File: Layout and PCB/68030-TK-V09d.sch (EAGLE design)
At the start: 73 parts, among them IC10 74HCT245DW, IC11 74HCT245DW, IC4 74HCT245DW, IC5 74HCT245DW, IC6 74HCT245DW, IC8 74HCT245DW, IC9 74HCT245DW, X1 FABC96R

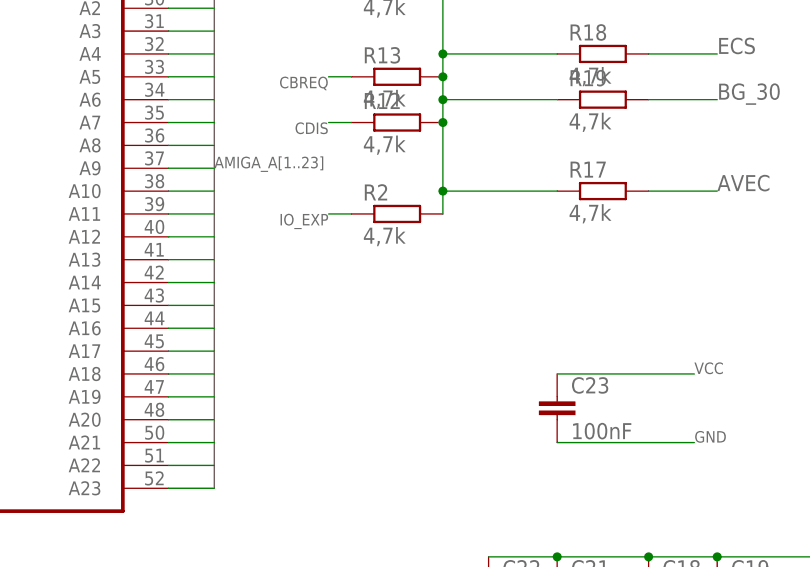
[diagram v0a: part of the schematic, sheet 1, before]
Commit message: Cache-Disable-Option on PCB
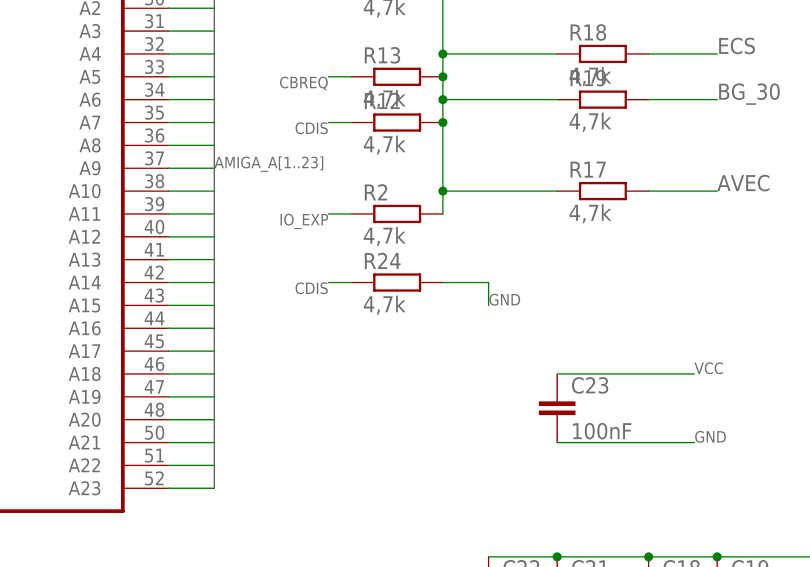
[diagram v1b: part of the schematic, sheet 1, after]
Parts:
- added R24: 4,7k, rcl:R-EU_R0603
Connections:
- net CDIS: now also R24.1
- net GND: now also R24.2
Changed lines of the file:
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@@
 <part name="R22" library="rcl" deviceset="R-EU_" device="R0603" value="4,7k"/>
 <part name="R23" library="rcl" deviceset="R-EU_" device="R0603" value="4,7k"/>
+<part name="R24" library="rcl" deviceset="R-EU_" device="R0603" value="4,7k"/>
 </parts>
 <sheets>
@@
 <instance part="R22" gate="G$1" x="-2.54" y="132.08"/>
 <instance part="R23" gate="G$1" x="-2.54" y="142.24"/>
+<instance part="R24" gate="G$1" x="-25.4" y="83.82"/>
 </instances>
 <busses>
@@
 <wire x1="132.08" y1="111.76" x2="137.16" y2="111.76" width="0.1524" layer="91"/>
 <label x="137.16" y="111.76" size="1.27" layer="95" xref="yes"/>
+</segment>
+<segment>
+<pinref part="R24" gate="G$1" pin="1"/>
+<wire x1="-30.48" y1="83.82" x2="-33.02" y2="83.82" width="0.1524" layer="91"/>
+<label x="-33.02" y="83.82" size="1.27" layer="95" rot="R180"/>
 </segment>
 </net>
@@
 <label x="7.62" y="66.04" size="1.27" layer="95"/>
 </segment>
-</net>
+<segment>
+<pinref part="R24" gate="G$1" pin="2"/>
+<wire x1="-20.32" y1="83.82" x2="-15.24" y2="83.82" width="0.1524" layer="91"/>
+<wire x1="-15.24" y1="83.82" x2="-15.24" y2="81.28" width="0.1524" layer="91"/>
+<label x="-15.24" y="81.28" size="1.27" layer="95"/>
+</segment>
+</net>

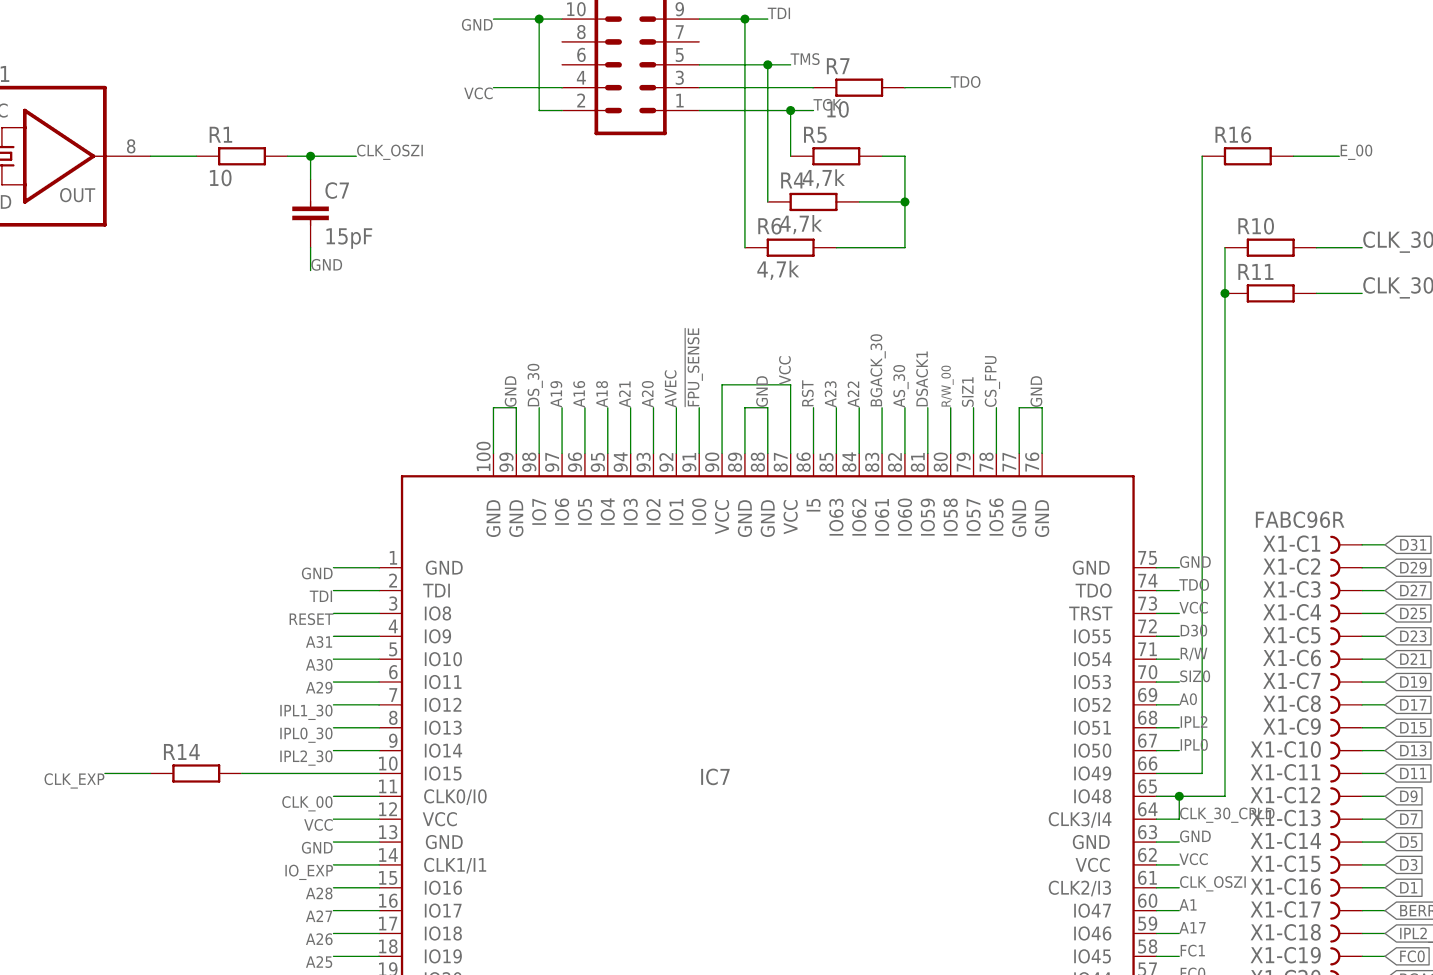
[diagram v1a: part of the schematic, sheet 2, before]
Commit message: Reset-Problem solved
The AMiga was not able to recover from a reste, because the e-clock was
not generated properly during reste.
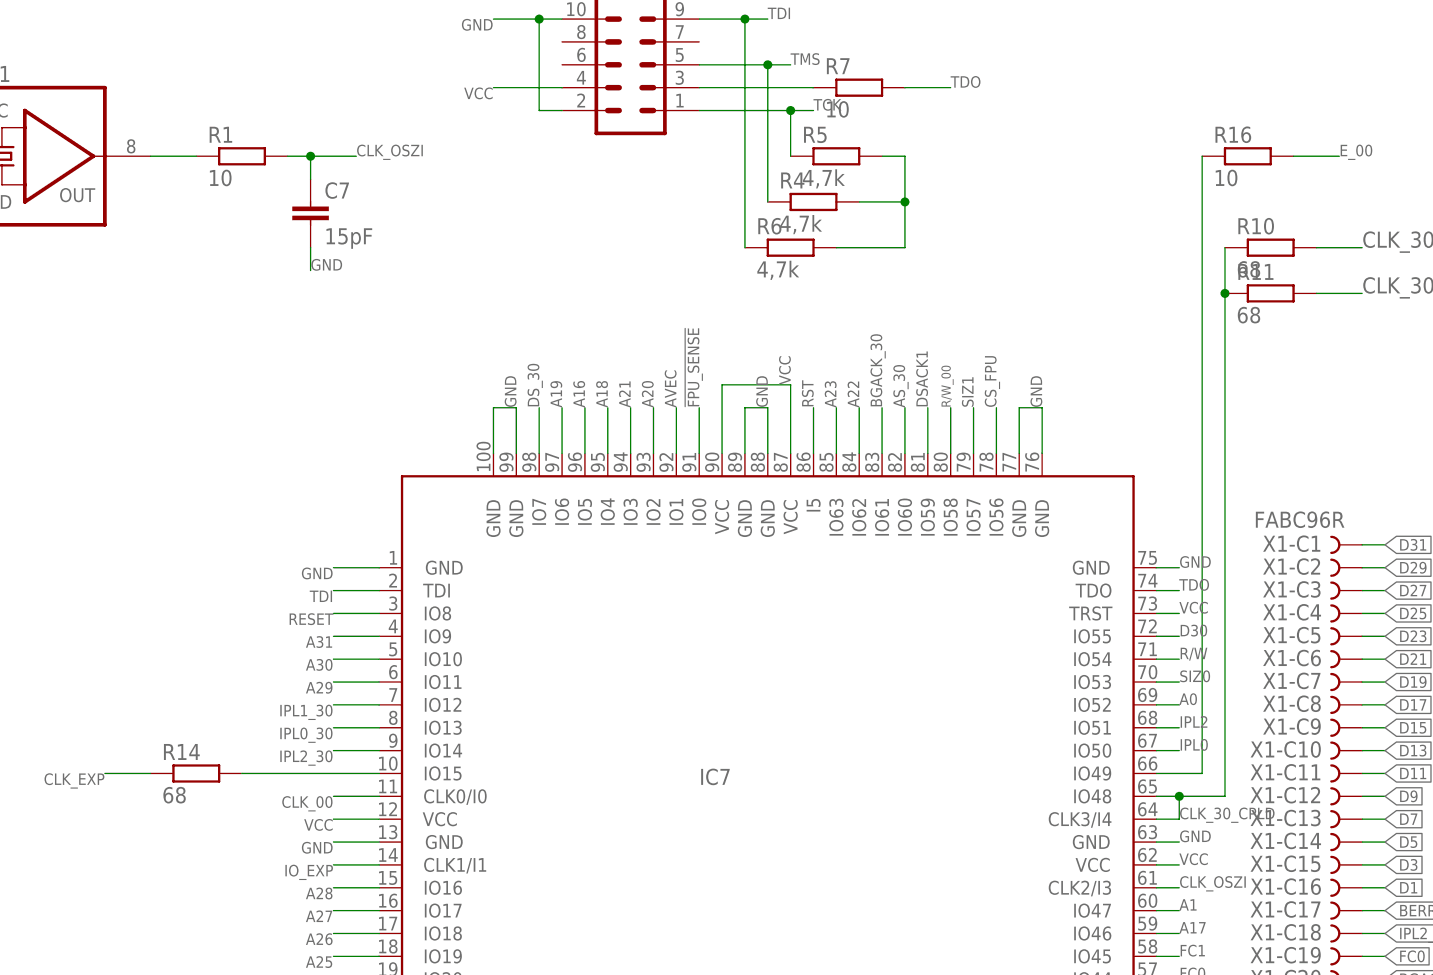
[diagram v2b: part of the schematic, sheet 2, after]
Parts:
- R10, R11, R14: value (none) -> 68
- R16: value (none) -> 10
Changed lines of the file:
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@@
 <?xml version="1.0" encoding="utf-8"?>
 <!DOCTYPE eagle SYSTEM "eagle.dtd">
-<eagle version="6.5.0">
+<eagle version="6.6.0">
 <drawing>
 <settings>
@@
 <part name="C27" library="rcl" deviceset="C-EU" device="C0603K" value="100nF"/>
 <part name="C28" library="rcl" deviceset="C-EU" device="C0603K" value="100nF"/>
-<part name="R10" library="rcl" deviceset="R-EU_" device="R0603"/>
-<part name="R11" library="rcl" deviceset="R-EU_" device="R0603"/>
-<part name="R14" library="rcl" deviceset="R-EU_" device="R0603"/>
-<part name="R16" library="rcl" deviceset="R-EU_" device="R0603"/>
+<part name="R10" library="rcl" deviceset="R-EU_" device="R0603" value="68"/>
+<part name="R11" library="rcl" deviceset="R-EU_" device="R0603" value="68"/>
+<part name="R14" library="rcl" deviceset="R-EU_" device="R0603" value="68"/>
+<part name="R16" library="rcl" deviceset="R-EU_" device="R0603" value="10"/>
 <part name="R17" library="rcl" deviceset="R-EU_" device="R0603" value="4,7k"/>
 <part name="RN3" library="resistor-dil" deviceset="4R-N" device="EXBV8V" value="4,7k"/>
